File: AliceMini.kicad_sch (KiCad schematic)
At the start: 25 parts, among them IC1 OPA1642AIDR

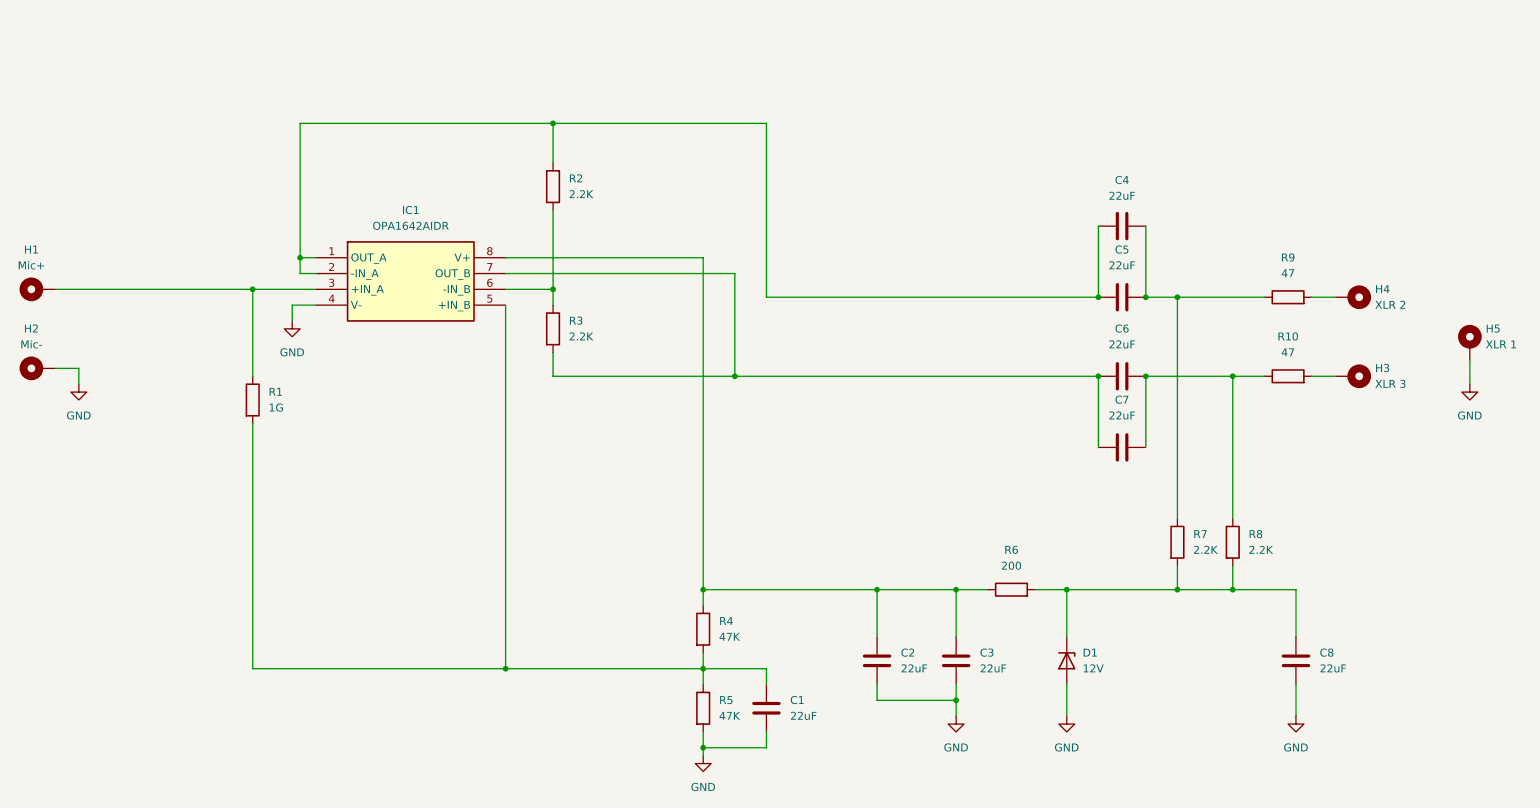
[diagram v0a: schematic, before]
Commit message: Reduce board size and snap to mm instead of mils
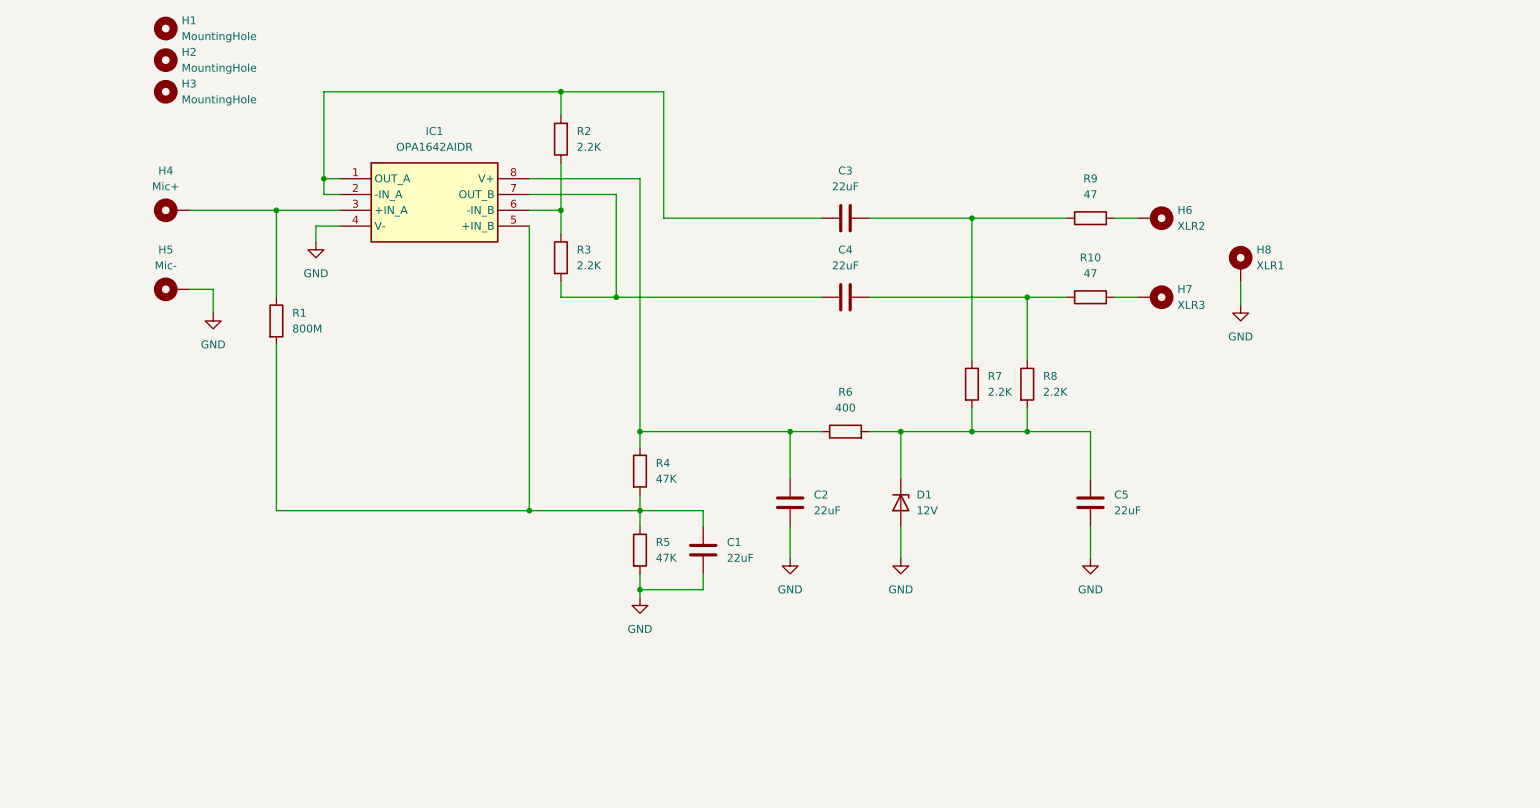
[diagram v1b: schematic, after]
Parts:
- removed C2, C4, C7: 22uF, Capacitor_SMD:C_2220_5750Metric, symbol Device:C
- added H1, H2, H3: MountingHole, MountingHole:MountingHole_2.2mm_M2, symbol Mechanical:MountingHole
- H4: renamed from H1; footprint TestPoint:TestPoint_THTPad_D3.0mm_Drill1.5mm -> TestPoint:TestPoint_THTPad_2.0x2.0mm_Drill1.0mm
- H5: renamed from H2; footprint TestPoint:TestPoint_THTPad_D3.0mm_Drill1.5mm -> TestPoint:TestPoint_THTPad_2.0x2.0mm_Drill1.0mm
- H6: renamed from H4; value XLR 2 -> XLR2; footprint TestPoint:TestPoint_THTPad_D3.0mm_Drill1.5mm -> TestPoint:TestPoint_THTPad_2.0x2.0mm_Drill1.0mm
- H7: renamed from H3; value XLR 3 -> XLR3; footprint TestPoint:TestPoint_THTPad_D3.0mm_Drill1.5mm -> TestPoint:TestPoint_THTPad_2.0x2.0mm_Drill1.0mm
- H8: renamed from H5; value XLR 1 -> XLR1; footprint TestPoint:TestPoint_THTPad_D3.0mm_Drill1.5mm -> TestPoint:TestPoint_THTPad_2.0x2.0mm_Drill1.0mm
- R1: value 1G -> 800M; footprint Resistor_SMD:R_0805_2012Metric -> Resistor_SMD:R_1206_3216Metric
- R6: value 200 -> 400
- renumbered C3 to C2, C5 to C3, C6 to C4, C8 to C5
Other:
- moved on the sheet: C1, C2, C3, C4, C5, D1, H4, H5, H6, H7, H8, IC1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

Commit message: fix: Updated high impedance resistor to 1G again
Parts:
- removed H1, H2, H3: MountingHole, MountingHole:MountingHole_2.2mm_M2, symbol Mechanical:MountingHole
- added C6, C7, C8: 10uF, Capacitor_SMD:C_1206_3216Metric, symbol Device:C
- C1, C2, C3, C4, C5: value 22uF -> 10uF; footprint Capacitor_SMD:C_2220_5750Metric -> Capacitor_SMD:C_1206_3216Metric
- R1: value 800M -> 1000M; footprint Resistor_SMD:R_1206_3216Metric -> Resistor_SMD:R_0805_2012Metric
- R10, R2, R3, R4, R5, R7, R8, R9: footprint Resistor_SMD:R_0805_2012Metric -> Resistor_SMD:R_0603_1608Metric
- R6: value 400 -> 470; footprint Resistor_SMD:R_0805_2012Metric -> Resistor_SMD:R_0603_1608Metric
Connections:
- net GND: now also C1.1, C2.1, C3.1, C8.1; no longer C1.2, C2.2, C5.2
- net at IC1.8 (V+), R4.1, R6.1: now also C2.2, C3.2; no longer C2.1
- net at IC1.5 (+IN_B), R1.2, R4.2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: now also C1.2; no longer C1.1
- net at IC1.1 (OUT_A), IC1.2 (-IN_A), R2.2: now also C4.1, C5.1; no longer C3.1
- net at R7.1, R9.1: now also C4.2, C5.2; no longer C3.2
- net at D1.1 (K), R6.2, R7.2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: now also C8.2; no longer C5.1
- net at IC1.7 (OUT_B), R3.2: now also C6.1, C7.1; no longer C4.1
- net at R10.1, R8.1: now also C6.2, C7.2; no longer C4.2
